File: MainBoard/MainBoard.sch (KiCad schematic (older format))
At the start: 5 parts, among them J1 DF40C-100DS-0.4V(51) _LFT, J2 DF40C-100DS-0.4V(51) _RFT (PN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, J3 HDMI_A, J4 Barrel_Jack, J7 USB_C_Receptacle

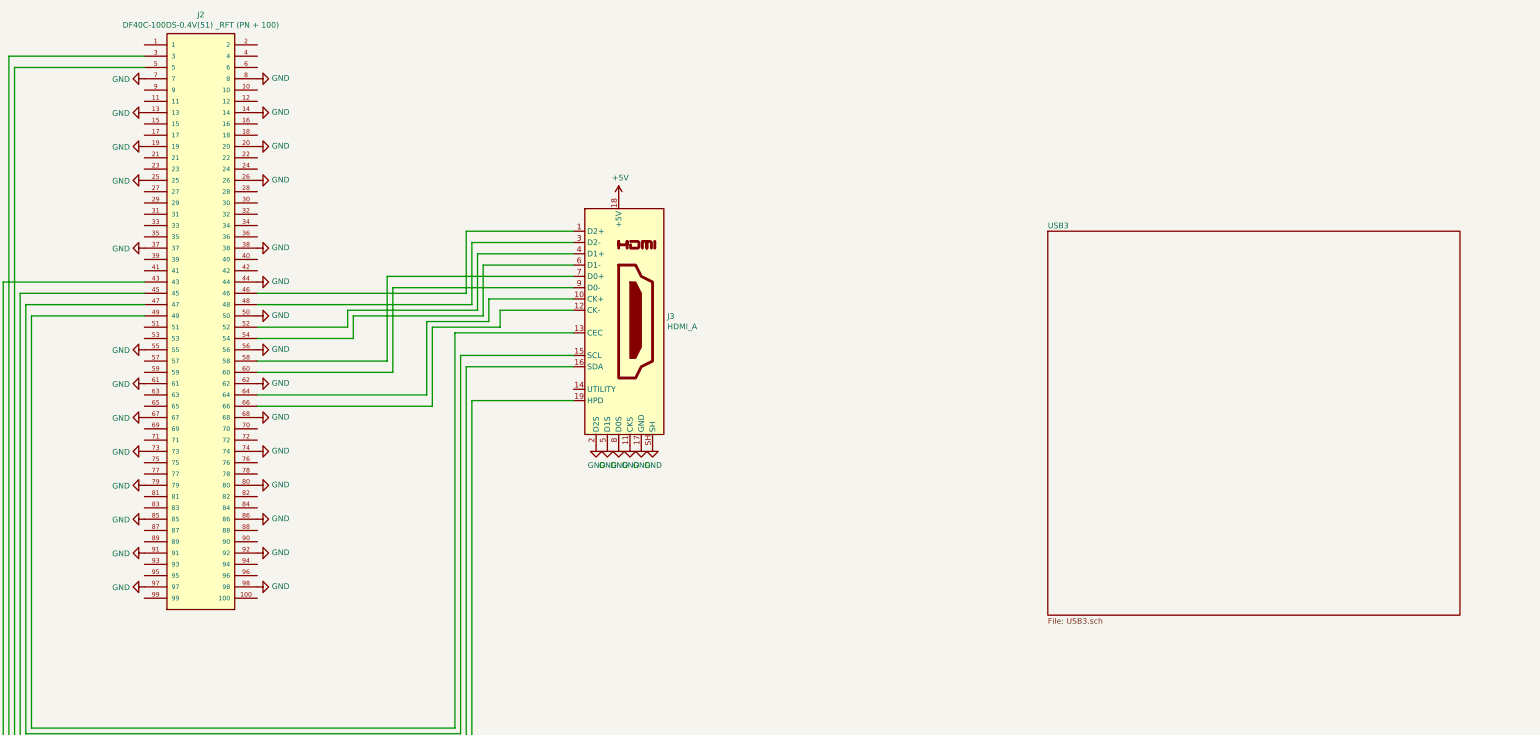
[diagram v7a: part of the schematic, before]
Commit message: add pcie nets, intearnal hub and ports
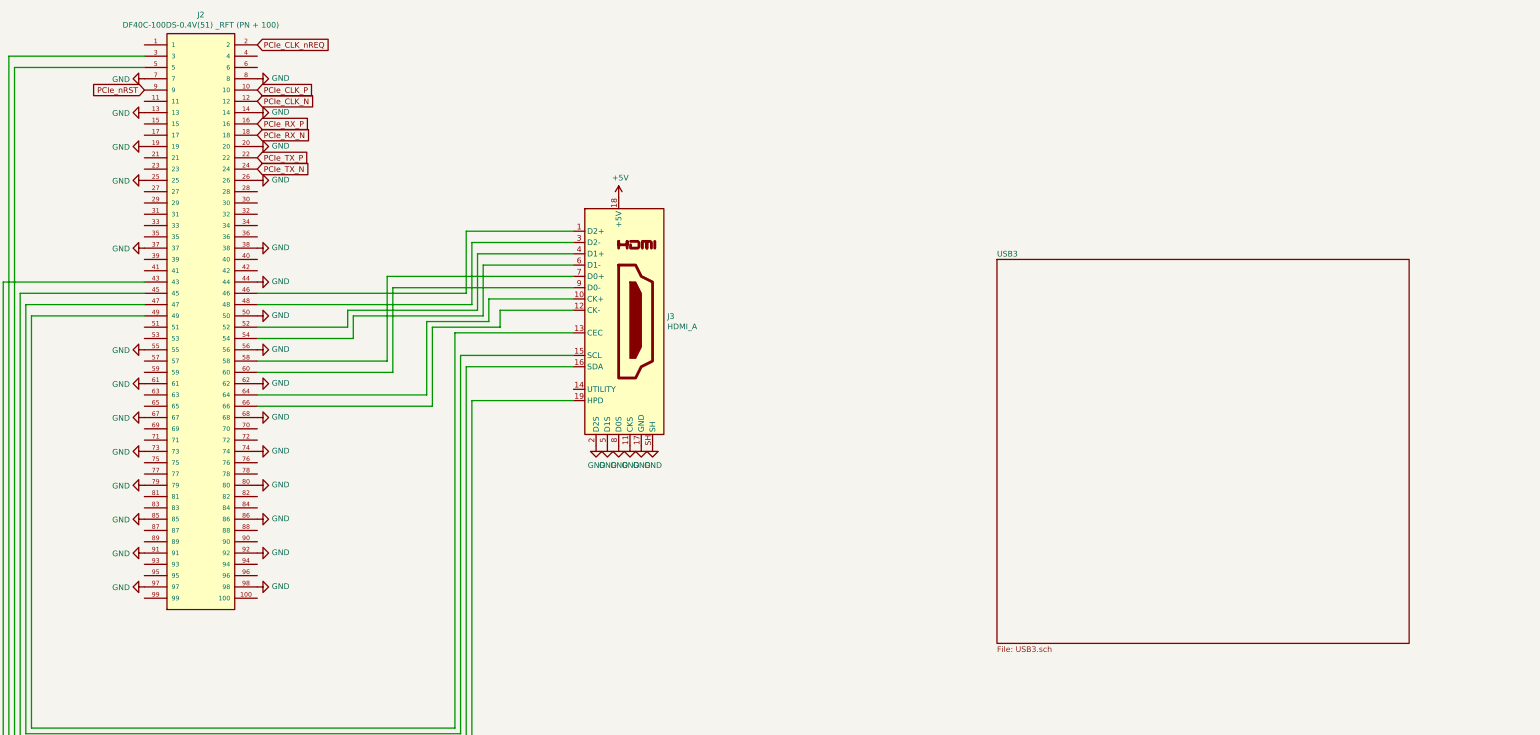
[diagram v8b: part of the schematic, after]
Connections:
- net PCIe_CLK_P: now reaches J2.10
- net PCIe_CLK_N: now reaches J2.12
- net PCIe_RX_P: now reaches J2.16
- net PCIe_RX_N: now reaches J2.18
- net PCIe_CLK_nREQ: now reaches J2.2
- net PCIe_TX_P: now reaches J2.22
- net PCIe_TX_N: now reaches J2.24
- net PCIe_nRST: now reaches J2.9
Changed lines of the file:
@@
 	1    0    0    -1
 $EndComp
-$Sheet
-S 15150 10350 3550 3550
-U 603B30DE
-F0 "Power_Delivery" 50
-F1 "Power.sch" 50
-F2 "HV_IN" I R 18700 10850 50
-F3 "5v_OUT" I R 18700 11000 50
-F4 "5v_IN" I R 18700 11150 50
-$EndSheet
 Wire Wire Line
 	20500 10750 19050 10750
@@
 	19050 10750 19050 10850
 Wire Wire Line
-	19050 10850 18700 10850
-Wire Wire Line
-	18700 11150 20250 11150
-Wire Wire Line
 	20250 11150 20250 10000
-$Comp
-L power:+5V #PWR0101
-U 1 1 603B66DB
-P 18700 11000
-F 0 "#PWR0101" H 18700 10850 50  0001 C CNN
-F 1 "+5V" V 18715 11128 50  0000 L CNN
-F 2 "" H 18700 11000 50  0001 C CNN
-F 3 "" H 18700 11000 50  0001 C CNN
-	1    18700 11000
-	0    1    1    0
-$EndComp
 Wire Wire Line
 	5350 6050 5800 6050
@@
 $EndComp
 $Sheet
-S 15950 3000 3650 3400
+S 15500 3250 3650 3400
 U 6042C255
 F0 "USB3" 50
@@
 Text GLabel 20250 9500 0    50   Input ~ 0
 USBCM
+$Comp
+L power:+5V #PWR0101
+U 1 1 603B66DB
+P 18700 11000
+F 0 "#PWR0101" H 18700 10850 50  0001 C CNN
+F 1 "+5V" V 18715 11128 50  0000 L CNN
+F 2 "" H 18700 11000 50  0001 C CNN
+F 3 "" H 18700 11000 50  0001 C CNN
+	1    18700 11000
+	0    1    1    0
+$EndComp
+Wire Wire Line
+	18700 11150 20250 11150
+Wire Wire Line
+	19050 10850 18700 10850
+$Sheet
+S 15150 10350 3550 3550
+U 603B30DE
+F0 "Power_Delivery" 50
+F1 "Power.sch" 50
+F2 "HV_IN" I R 18700 10850 50
+F3 "5v_OUT" I R 18700 11000 50
+F4 "5v_IN" I R 18700 11150 50
+$EndSheet
+Text GLabel 8950 1350 2    50   Input ~ 0
+PCIe_CLK_nREQ
+Text GLabel 7950 1750 0    50   Input ~ 0
+PCIe_nRST
+Text GLabel 8950 1750 2    50   Input ~ 0
+PCIe_CLK_P
+Text GLabel 8950 1850 2    50   Input ~ 0
+PCIe_CLK_N
+Text GLabel 8950 2050 2    50   Input ~ 0
+PCIe_RX_P
+Text GLabel 8950 2150 2    50   Input ~ 0
+PCIe_RX_N
+Text GLabel 8950 2350 2    50   Input ~ 0
+PCIe_TX_P
+Text GLabel 8950 2450 2    50   Input ~ 0
+PCIe_TX_N
 $EndSCHEMATC
